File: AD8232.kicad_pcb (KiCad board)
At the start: 2 copper layers, 33 parts, among them J1 Conn_01x03, J2 Conn_01x06, J3 AudioJack3, M1 AD8232

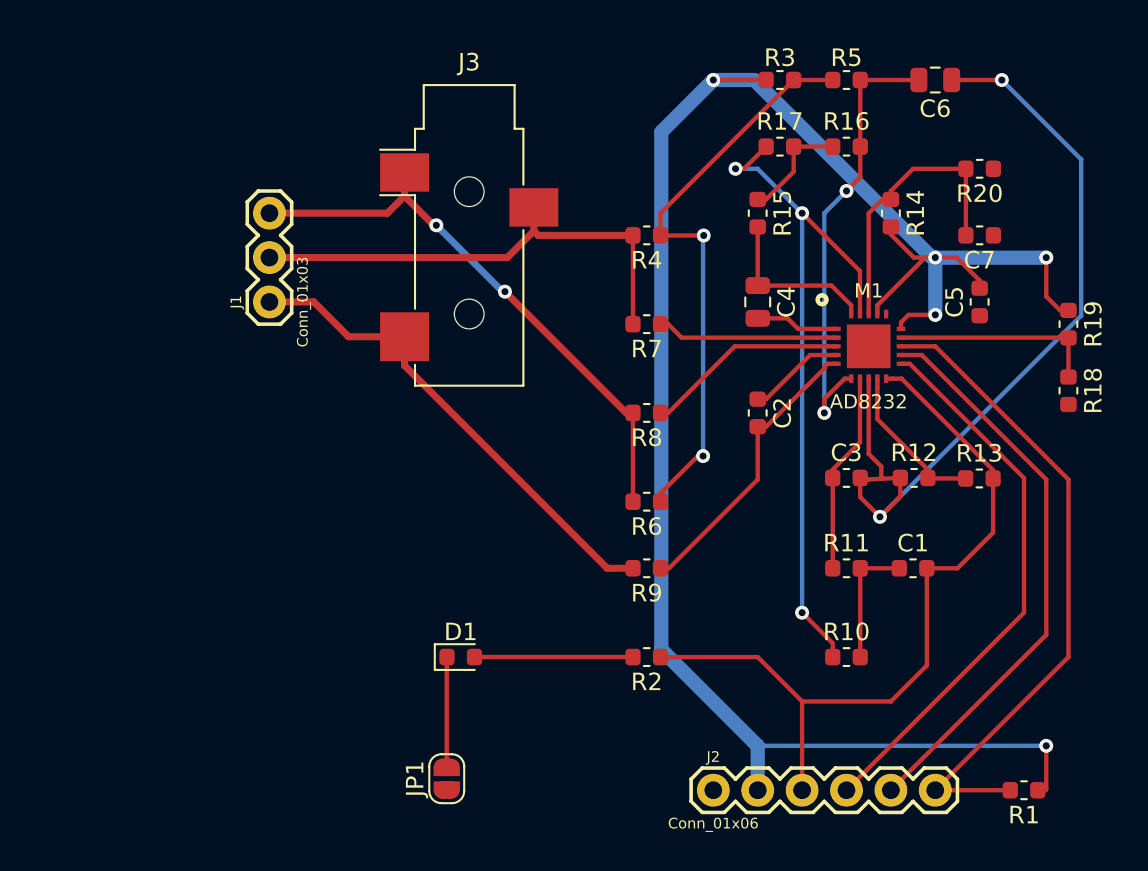
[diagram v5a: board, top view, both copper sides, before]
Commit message: conectar GND
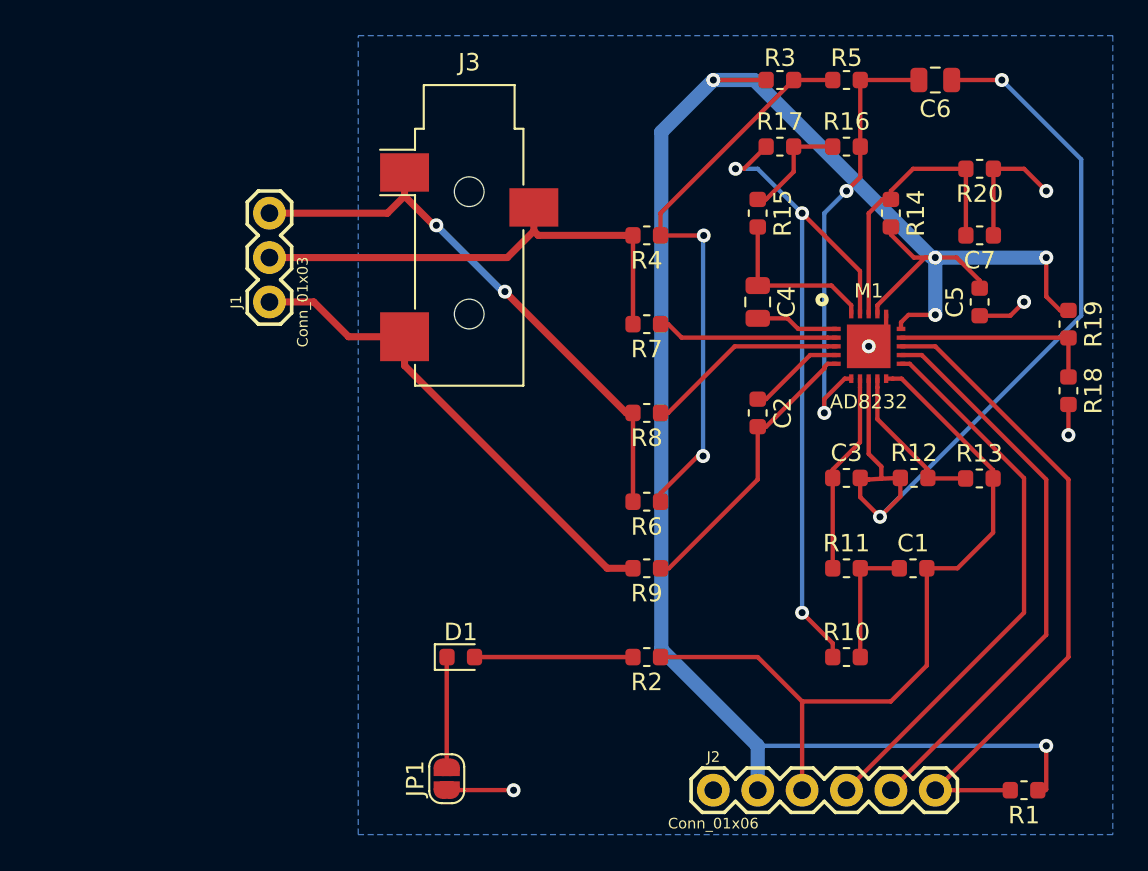
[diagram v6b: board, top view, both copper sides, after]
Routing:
- net GND: track 0.00 -> 18.1 mm, vias 0 -> 5
- added copper zone on B.Cu, net GND
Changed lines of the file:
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@@
     (thickness 1.6)
     (drawings 0)
-    (tracks 196)
+    (tracks 211)
     (zones 0)
     (modules 33)
@@
     )
   )
+  (via (at 162.56 88.9) (size 0.8) (drill 0.4) (layers F.Cu B.Cu) (net 10))
   (segment (start 158.75 114.3) (end 158.75 109.22) (width 0.25) (layer F.Cu) (net 1))
   (segment (start 156.21 106.68) (end 150.6475 106.68) (width 0.25) (layer F.Cu) (net 1))
@@
   (segment (start 172.72 86.0475) (end 173.515 86.8425) (width 0.25) (layer F.Cu) (net 9))
   (segment (start 172.72 83.82) (end 172.72 86.0475) (width 0.25) (layer F.Cu) (net 9))
+  (segment (start 163.55822 87.90178) (end 163.55822 87.05088) (width 0.25) (layer F.Cu) (net 10))
+  (segment (start 162.56 88.9) (end 163.55822 87.90178) (width 0.25) (layer F.Cu) (net 10))
+  (via (at 142.24 114.3) (size 0.8) (drill 0.4) (layers F.Cu B.Cu) (net 10))
+  (segment (start 142.231913 114.291913) (end 142.24 114.3) (width 0.25) (layer F.Cu) (net 10))
+  (segment (start 138.414751 114.291913) (end 142.231913 114.291913) (width 0.25) (layer F.Cu) (net 10))
+  (via (at 173.99 93.98) (size 0.8) (drill 0.4) (layers F.Cu B.Cu) (net 10))
+  (via (at 171.45 86.36) (size 0.8) (drill 0.4) (layers F.Cu B.Cu) (net 10))
+  (via (at 172.72 80.01) (size 0.8) (drill 0.4) (layers F.Cu B.Cu) (net 10))
+  (segment (start 173.99 92.2275) (end 173.99 93.98) (width 0.25) (layer F.Cu) (net 10))
+  (segment (start 170.6625 87.1475) (end 171.45 86.36) (width 0.25) (layer F.Cu) (net 10))
+  (segment (start 168.91 87.1475) (end 170.6625 87.1475) (width 0.25) (layer F.Cu) (net 10))
+  (segment (start 171.45 78.74) (end 172.72 80.01) (width 0.25) (layer F.Cu) (net 10))
+  (segment (start 169.6975 78.74) (end 171.45 78.74) (width 0.25) (layer F.Cu) (net 10))
+  (segment (start 169.6975 78.74) (end 169.6975 82.55) (width 0.25) (layer F.Cu) (net 10))
   (segment (start 165.4325 73.66) (end 162.0775 73.66) (width 0.25) (layer F.Cu) (net 11))
   (segment (start 162.0775 73.66) (end 162.0775 77.47) (width 0.25) (layer F.Cu) (net 11))
@@
   (segment (start 156.685 80.4925) (end 156.21 80.4925) (width 0.25) (layer F.Cu) (net 27))
   (segment (start 158.2675 77.47) (end 158.2675 78.91) (width 0.25) (layer F.Cu) (net 27))
+  (zone (net 10) (net_name GND) (layer B.Cu) (hatch edge 0.508)
+    (connect_pads (clearance 0.508))
+    (min_thickness 0.254)
+    (fill yes (arc_segments 32) (thermal_gap 0.508) (thermal_bridge_width 0.508))
+    (polygon
+      (pts
+        (xy 176.53 116.84) (xy 133.35 116.84) (xy 133.35 71.12) (xy 176.53 71.12)
+      )
+    )
+  )
 )

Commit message: definir corte de orilla de PCB
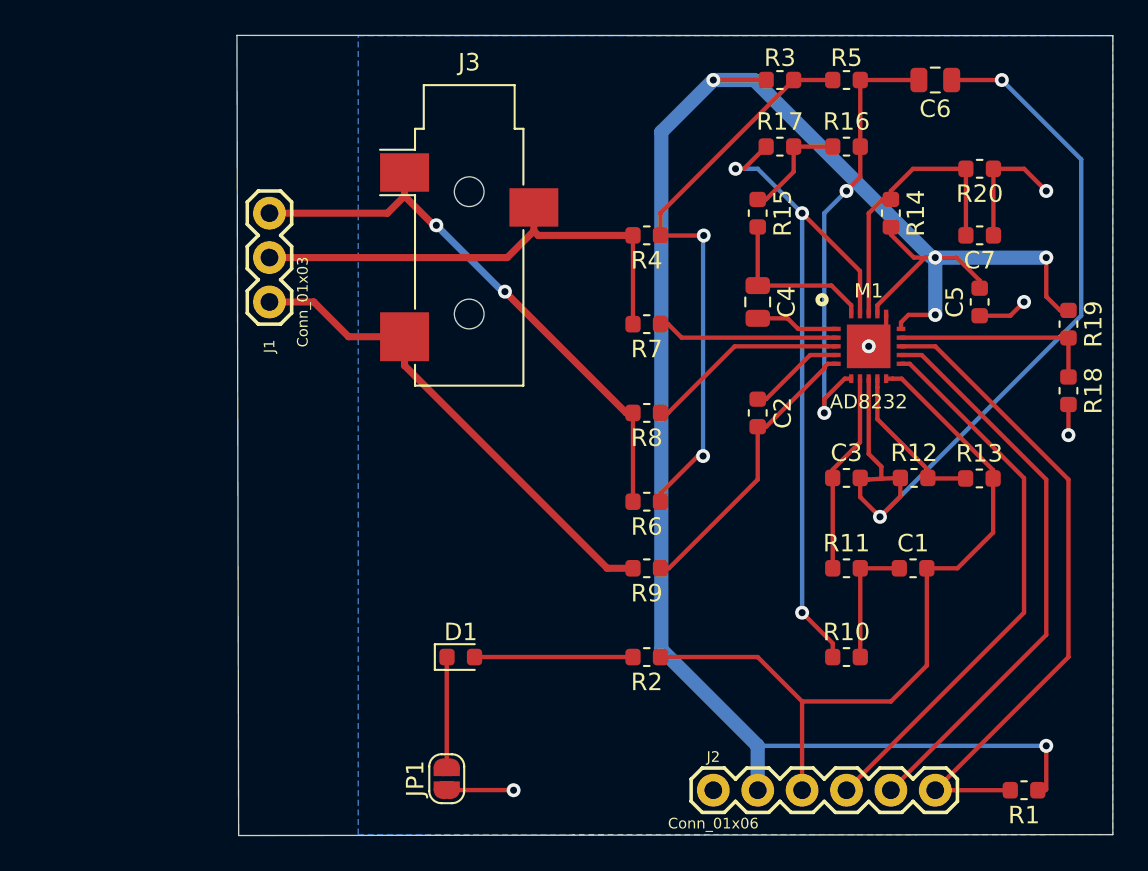
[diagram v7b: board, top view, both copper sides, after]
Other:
- board outline added: 50.1 x 45.8 mm
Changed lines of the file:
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@@
   (general
     (thickness 1.6)
-    (drawings 0)
+    (drawings 4)
     (tracks 211)
     (zones 0)
@@
     (tags "PLATED THROUGH HOLE - 3 PIN")
     (attr virtual)
-    (fp_text reference J1 (at 0 -1.905 90) (layer F.SilkS)
+    (fp_text reference J1 (at -2.54 0 90) (layer F.SilkS)
       (effects (font (size 0.6096 0.6096) (thickness 0.127)))
     )
@@
     )
   )
+  (gr_line (start 126.506516 116.89285) (end 176.53 116.84) (layer Edge.Cuts) (width 0.05))
+  (gr_line (start 126.410122 71.105802) (end 126.506516 116.89285) (layer Edge.Cuts) (width 0.05))
+  (gr_line (start 176.53 71.12) (end 126.410122 71.105802) (layer Edge.Cuts) (width 0.05))
+  (gr_line (start 176.53 116.84) (end 176.53 71.12) (layer Edge.Cuts) (width 0.05))
   (via (at 162.56 88.9) (size 0.8) (drill 0.4) (layers F.Cu B.Cu) (net 10))
   (segment (start 158.75 114.3) (end 158.75 109.22) (width 0.25) (layer F.Cu) (net 1))
